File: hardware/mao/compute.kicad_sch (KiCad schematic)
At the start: 46 parts, among them J201 TAG, U201 ESP32-S3-WROOM-1-N8R2, U202 TCA6408ARGTR

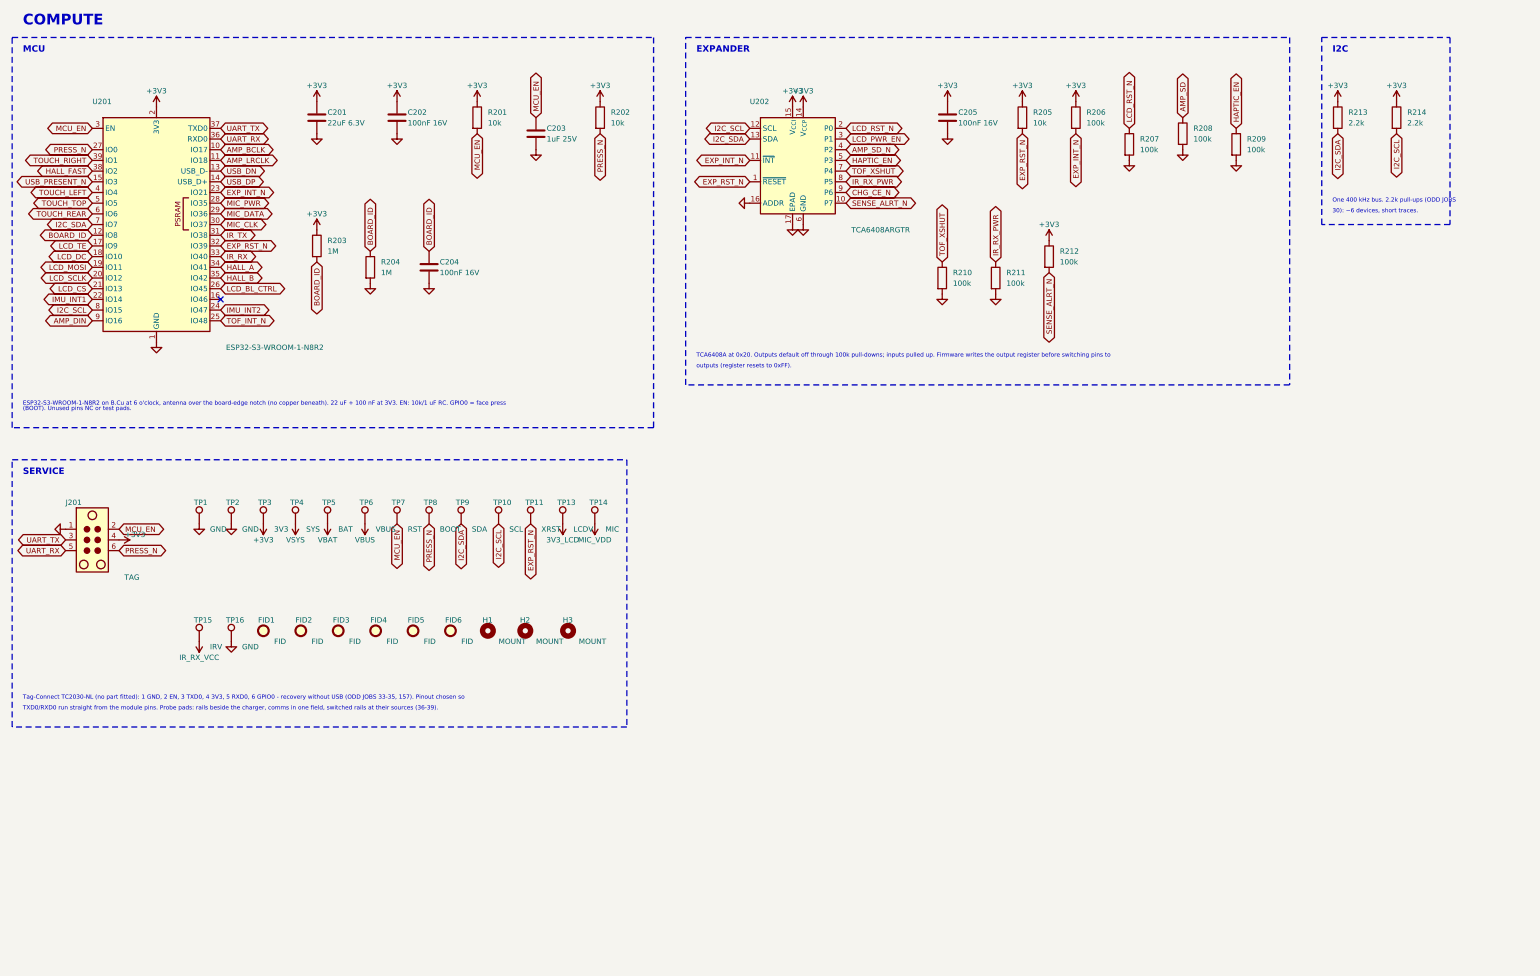
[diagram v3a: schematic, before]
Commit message: MAO A0 schematic: one frame per block, wired local nets, no overprinted names
ODD JOBS audit 2, X8 (rules 187, 188):
- Parts added late (C111, R117, R507) join their block's frame instead of opening a duplicate frame
  with a copy of its note that ran over the neighbours.
- A two-pin part on a net that only joins it to one side pin of its block's IC is wired to that pin
  (the pin's label still names the net, so board, rules and procedures keep their names); feedback and
  UVLO-style dividers hang off their pin as a divider column. Columns step so no wire crosses a part.
- Adjacent pins on one rail share one rail symbol, joined by a wire; a sideways rail symbol keeps its
  name on its own row; turned passives, LEDs and diodes keep their reference and value off the body.
- Rail-source declarations sit in their own frame in the layout flow, not over the title block.
- Two stale notes corrected (C105 distance to VIN, R204 A0 voltage); board fields synced.

ERC 0, DRC 0 / 0 / parity 0.

Co-Authored-By: Claude Opus 5.5 <noreply@anthropic.com>
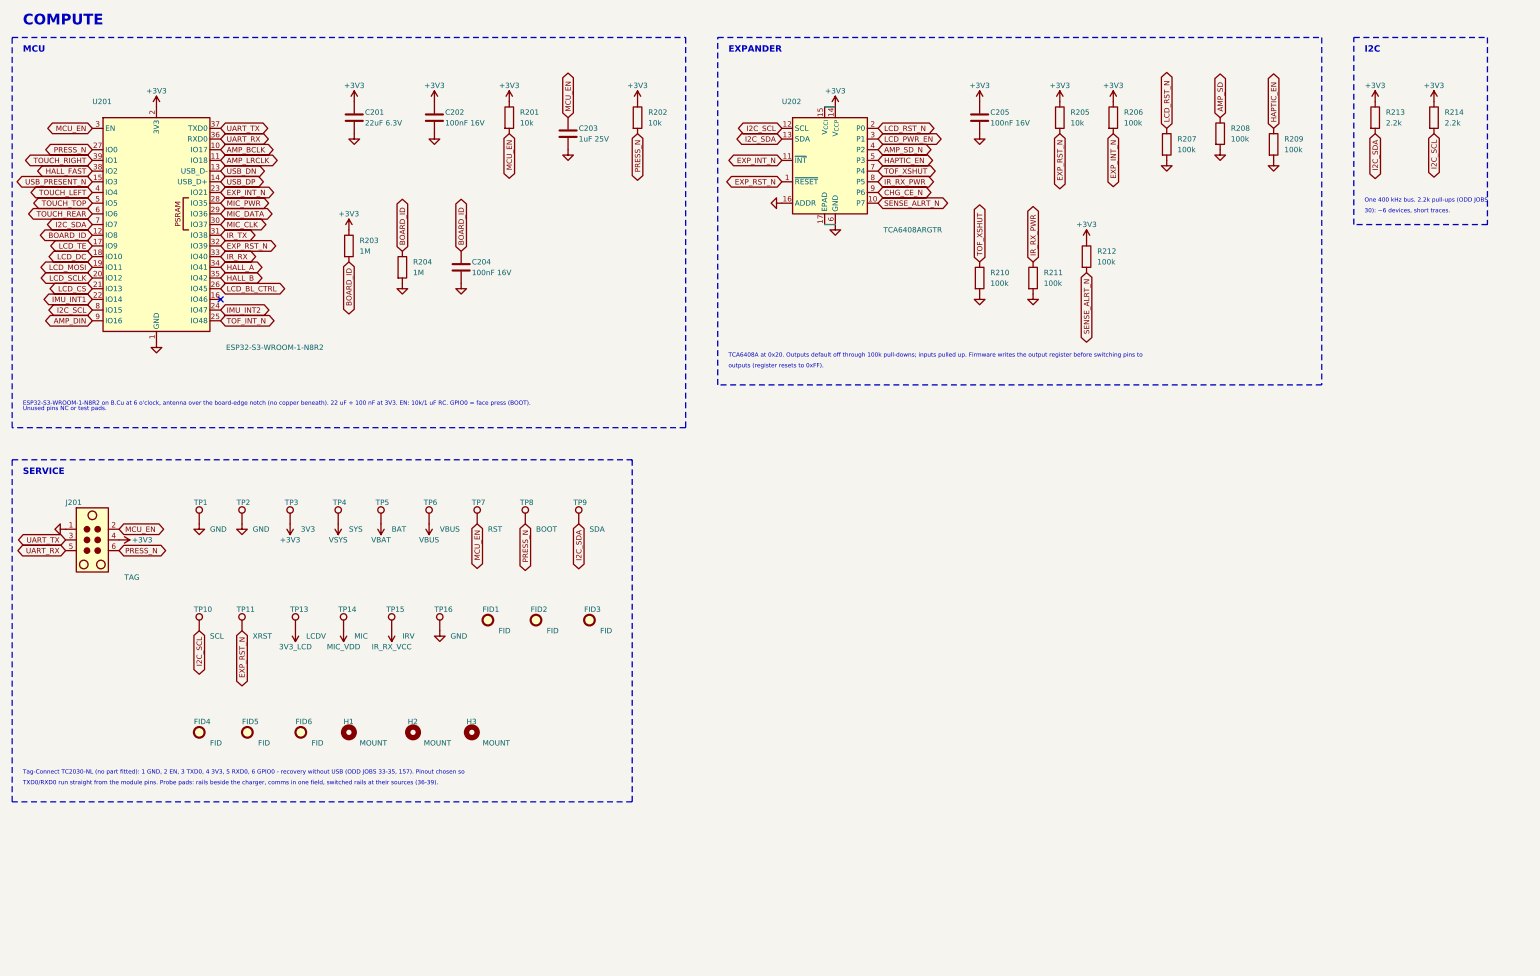
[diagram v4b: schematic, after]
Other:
- note added: "ESP32-S3-WROOM-1-N8R2 on B.Cu at 6 o'clock, antenna over the board-edge notch (no copper beneath). 22 uF + 100 nF at 3V3. EN: 10k/1 uF RC. GPIO0 = face press (BOOT)."
- note added: "Unused pins NC or test pads."
- note removed: "(BOOT). Unused pins NC or test pads."
- note removed: "ESP32-S3-WROOM-1-N8R2 on B.Cu at 6 o'clock, antenna over the board-edge notch (no copper beneath). 22 uF + 100 nF at 3V3. EN: 10k/1 uF RC. GPIO0 = face press"
- moved on the sheet: C201, C202, C203, C204, C205, FID1, FID2, FID3, FID4, FID5, FID6, H1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

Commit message: MAO A0 audit 3 fixes: VSYS feed un-necked, speaker lines over VSYS, silk leaders to their parts
Electrical audit 3 (no blocker; issue I-1):
- 11 o'clock panel tab 320 -> 328 deg: its keep-out necked the L3 VSYS band to 0.27 mm beside H1
- via-free corner where the VSYS branch turns into the backlight bar (a C205/U202 via left 0.26 mm)
- plane_check: GND and rail regions refilled at 0.5 mm minimum width must not split (necks fail
  the build); the +3V3 mesh is reported
- self-test board_id upper limit 1700 -> 1720 mV (the 3.32 V rail corner reached 1.697 V)
- comments: rail 3.10-3.32 V, AW9364 dropout, TPS22919 turn-on vs rise, panel clock, Kconfig help
- D101 drawn as a unidirectional TVS (zener glyph); module +3V3 via on C202's branch axis

ODD JOBS audit 3 (0 FAIL; recommended fixes):
- VSYS branch extended under both speaker lines (they sat over the VSYS/+3V3 zone gap); LCD_RST_N
  off L3; L3/L4 broadside 17.4 -> 13.8 mm
- EXP_RST_N's leg to TP11 designed on L3 (left to the router it detoured)
- leaders end 0.3 mm off their own part, at least 0.1 mm nearer it than any other part
- no silk text on touch-electrode copper (silk.py, mao_labels.py, check_silk_text.py): REAR and
  MIC moved
- schematic note lines on a 2.54 mm pitch (snapped 2.29 mm printed pairs that touched); tail note
- back identity on a reserved via-free spot; RSSI check with and without the LRA; drawing text
- final board: DRC 0/0/0, planes whole, no rail neck under 0.5 mm, silk 83 texts 0 findings,
  mech 0, 205 vias, 921 segments on 45 degrees; firmware 5 builds 0 warnings, 240 host checks;
  merge patch re-verified on b17187e

Co-Authored-By: Claude Opus 5.5 <noreply@anthropic.com>
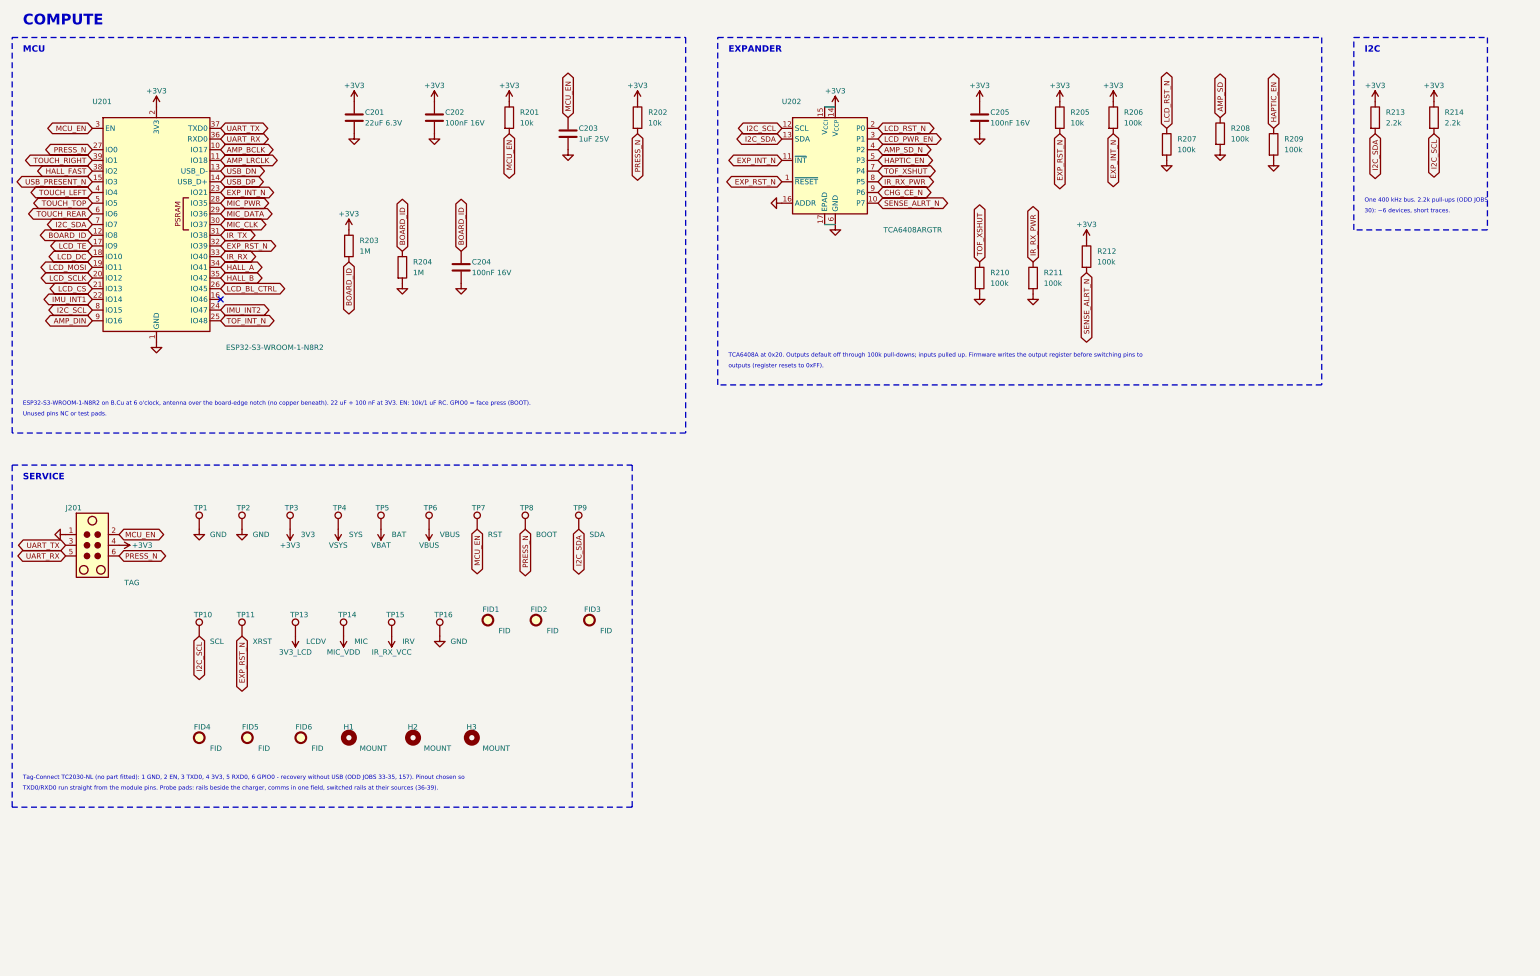
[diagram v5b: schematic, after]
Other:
- moved on the sheet: FID4, FID5, FID6, H1, H2, H3, J201, TP1, TP10, TP11, TP13, TP14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
